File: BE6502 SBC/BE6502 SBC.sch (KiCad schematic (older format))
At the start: 35 parts, among them J1 Expansion, J3 BARREL_JACK, M1 Mounting, M2 Mounting, M3 Mounting, M4 Mounting, SW1 RESET, SW2 RESET, SW3 RESET, SW4 RESET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

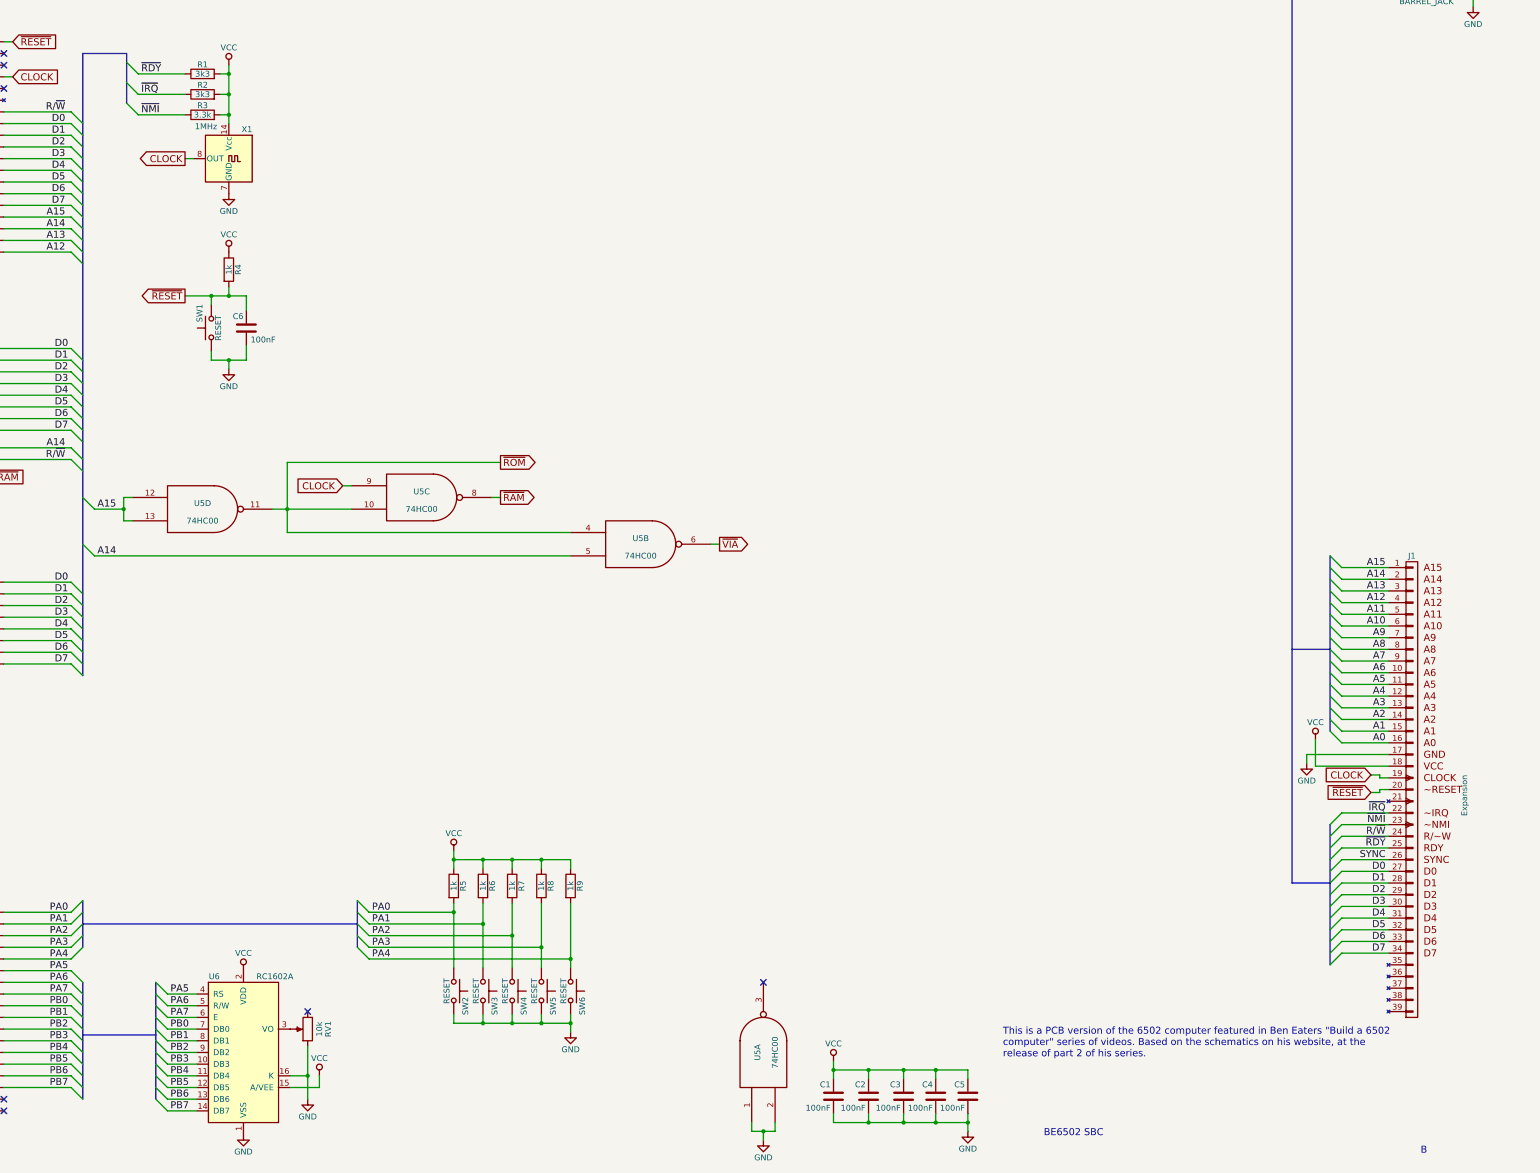
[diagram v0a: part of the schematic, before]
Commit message: Added LEDs
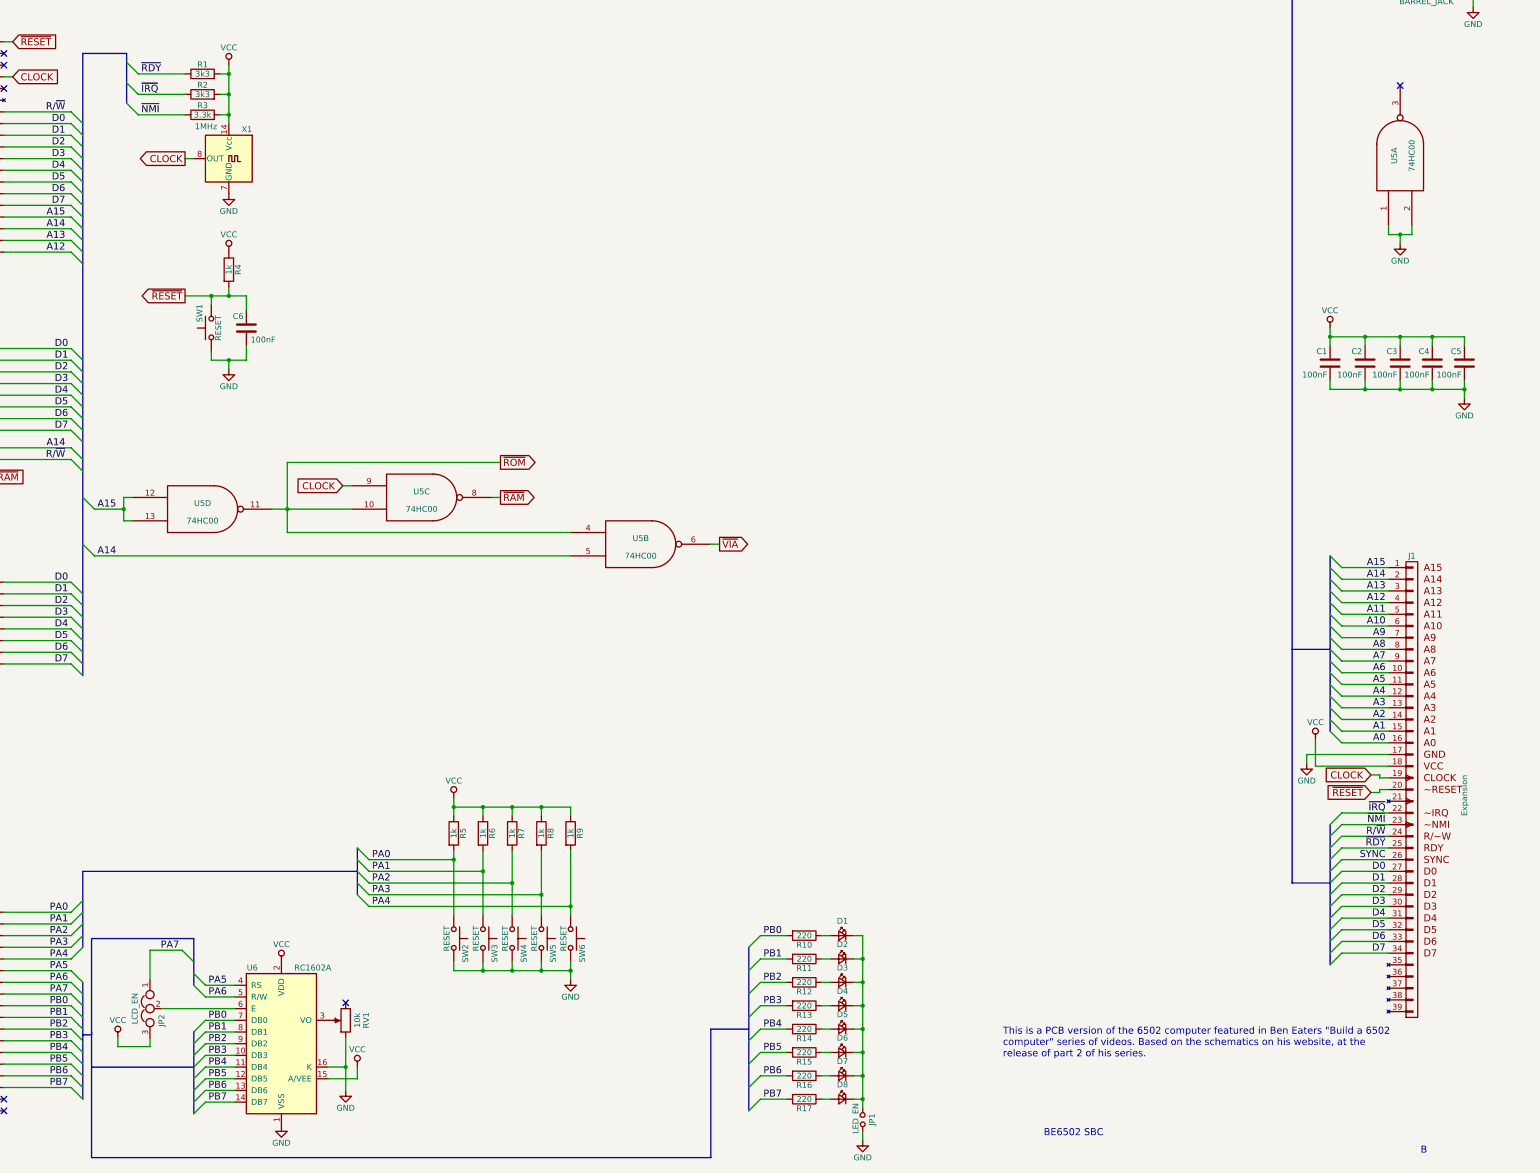
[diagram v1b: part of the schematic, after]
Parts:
- added D1, D2, D3, D4, D5, D6, D7, D8: LED, symbol LED_Small
- added JP1: LED_EN, symbol Jumper_NO_Small
- added JP2: LCD_EN, symbol Jumper_NC_Dual
- added R10, R11, R12, R13, R14, R15, R16, R17: 220, Resistors_THT:R_Axial_DIN0207_L6.3mm_D2.5mm_P10.16mm_Horizontal, symbol R
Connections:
- net GND: now also JP1.1
- net PA7: now also JP2.1; no longer U6.6 (E)
- net PB0: now also R10.2
- net PB1: now also R11.2
- net PB2: now also R12.2
- net PB3: now also R13.2
- net PB4: now also R14.2
- net PB5: now also R15.2
- net PB6: now also R16.2
- net PB7: now also R17.2
- net VCC: now also JP2.3
- new net: JP2.2, U6.6 (E)
- new net: D1.1 (K), D2.1 (K), D3.1 (K), D4.1 (K), D5.1 (K), D6.1 (K), D7.1 (K), D8.1 (K), JP1.2
- new net: D8.2 (A), R17.1
- new net: D7.2 (A), R16.1
- new net: D6.2 (A), R15.1
- new net: D5.2 (A), R14.1
- new net: D4.2 (A), R13.1
- new net: D3.2 (A), R12.1
- new net: D2.2 (A), R11.1
- new net: D1.2 (A), R10.1
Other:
- moved on the sheet: C1, C2, C3, C4, C5, R5, R6, R7, R8, R9, RV1, SW2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

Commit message: Component placement
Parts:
- added J2: CLOCK_SEL, Pin_Headers:Pin_Header_Angled_1x04_Pitch2.54mm, symbol Conn_01x04
- D1, D2, D3, D4, D5, D6, D7, D8: footprint (none) -> LEDs:LED_D5.0mm
- J1: footprint (none) -> Pin_Headers:Pin_Header_Angled_1x39_Pitch2.54mm
- JP1: footprint (none) -> Pin_Headers:Pin_Header_Straight_1x02_Pitch2.54mm
- JP2: footprint (none) -> Pin_Headers:Pin_Header_Straight_1x03_Pitch2.54mm
- RV1: footprint (none) -> Potentiometers:Potentiometer_Trimmer_Bourns_3296W
- SW1: footprint (none) -> Buttons_Switches_THT:SW_PUSH_6mm
- SW2: value RESET -> MIDDLE; footprint (none) -> Buttons_Switches_THT:SW_PUSH_6mm
- SW3: value RESET -> UP; footprint (none) -> Buttons_Switches_THT:SW_PUSH_6mm
- SW4: value RESET -> DOWN; footprint (none) -> Buttons_Switches_THT:SW_PUSH_6mm
- SW5: value RESET -> LEFT; footprint (none) -> Buttons_Switches_THT:SW_PUSH_6mm
- SW6: value RESET -> RIGHT; footprint (none) -> Buttons_Switches_THT:SW_PUSH_6mm
- U1, U4: footprint (none) -> Housings_DIP:DIP-40_W15.24mm_Socket_LongPads
- U2, U3: footprint Housings_DIP:DIP-28_W15.24mm_Socket -> Housings_DIP:DIP-28_W15.24mm_Socket_LongPads
- U5: footprint (none) -> Housings_DIP:DIP-14_W7.62mm_Socket_LongPads
- U6: footprint Displays:RC1602A -> Displays:WC1602A
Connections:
- net CLOCK: now also J2.3 (Pin_3); no longer X1.8 (OUT)
- net GND: now also J2.4 (Pin_4)
- net VCC: now also J2.1 (Pin_1)
- new net: J2.2 (Pin_2), X1.8 (OUT)
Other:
- moved on the sheet: U5B, U5C, U5D, X1

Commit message: Layout done
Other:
- moved on the sheet: U5B
